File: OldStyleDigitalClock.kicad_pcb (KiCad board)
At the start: 2 copper layers, 155 x 85 mm, 89 parts, among them J1 USB_A_OUT, J2 USB_A_OUT, J3 USB_C_IN, SW1 Set minutes, SW2 Set hours, U1 CD4071BM, U10 CD4026BNSR, U11 NE555D, U12 CD4060BM, U13 CD4017BM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

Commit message: Reduced C13 value to avoid visible flickering
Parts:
- C13: value 0.047 uF -> 22 nF

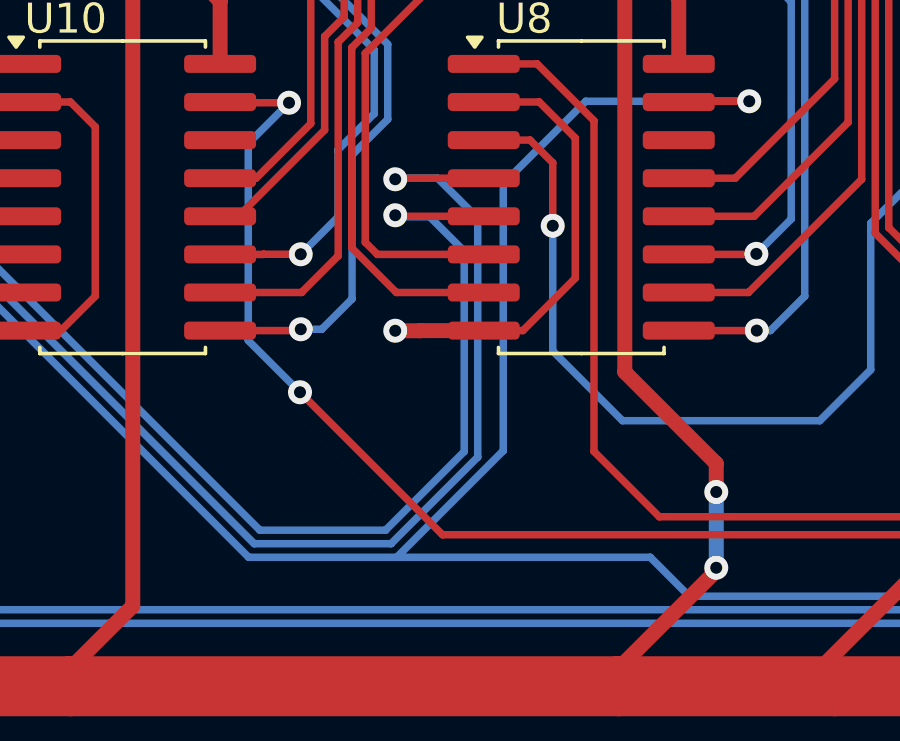
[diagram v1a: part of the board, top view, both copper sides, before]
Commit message: Added missing reset connection for low digit of the hours
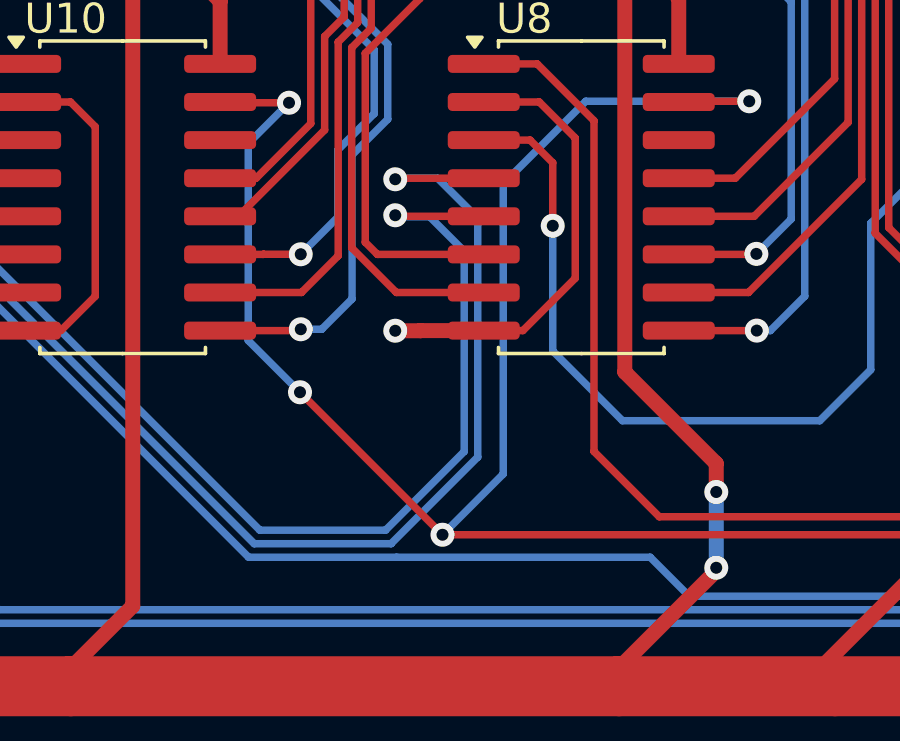
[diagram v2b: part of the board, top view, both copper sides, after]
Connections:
- U8 pad 15: MR -> Net-(U10-RESET)
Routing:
- net MR: track 192.2 -> 166.6 mm, vias 3 -> 2
- net Net-(U10-RESET): track 84.5 -> 108.7 mm, vias 2 -> 4

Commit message: Restored old Rs value of 300k
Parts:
- R_{S}1: value 200 kΩ -> 300 kΩ

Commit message: Reduced C13 to 4.7 nF to account for stray capacitance and avoid flickering
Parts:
- C13: value 22 nF -> 4.7 nF

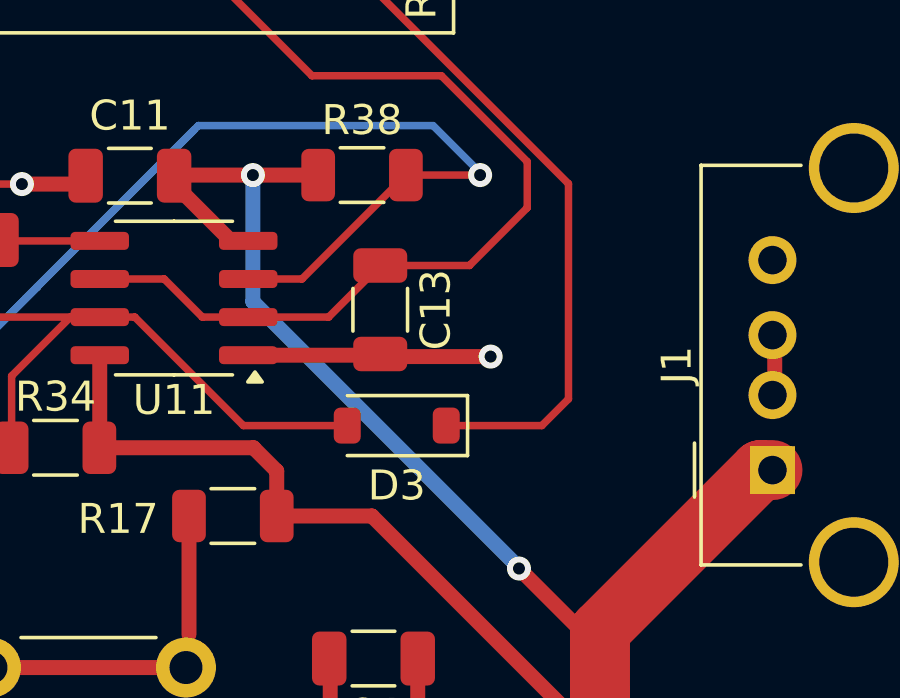
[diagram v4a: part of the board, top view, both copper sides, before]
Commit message: Minor PCB layout change to reduce traces stray capacitance
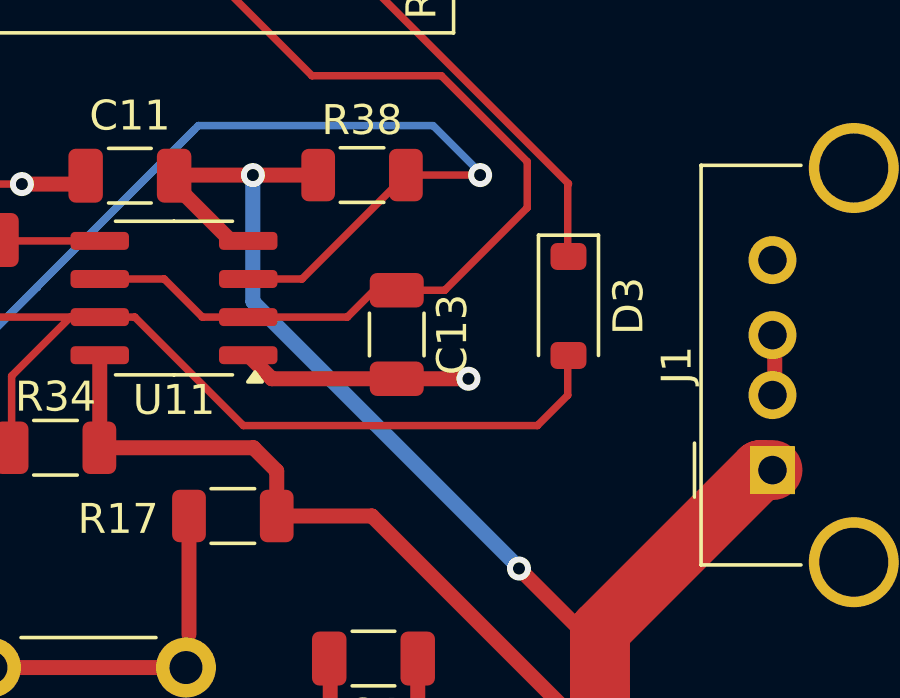
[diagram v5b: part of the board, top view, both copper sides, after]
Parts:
- moved D3 6.98 mm to (184.9, 70.5), turned to -90 degrees
- moved C13 0.99 mm to (179.2, 71.4)
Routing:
- net Net-(D3-K): track 26.7 -> 17.6 mm
- net Net-(D3-A): track 71.9 -> 81.0 mm

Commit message: Reduced C13 further while staying within the 555 limit of 100 kHz even when LDR may raise to several MΩ. This avoids flickering.
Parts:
- C13: value 4.7 nF -> 1 nF

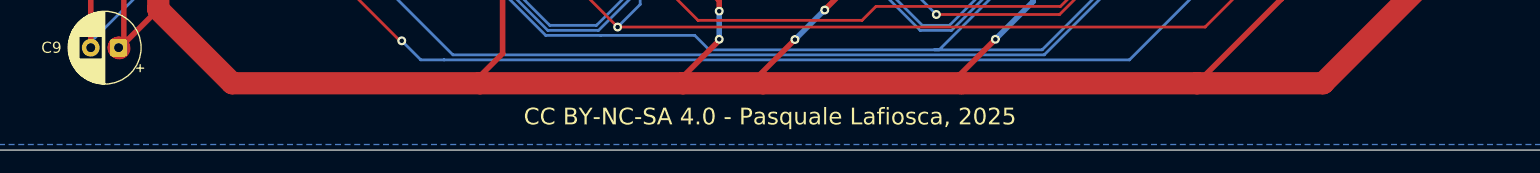
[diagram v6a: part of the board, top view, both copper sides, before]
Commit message: Added link in PCB description
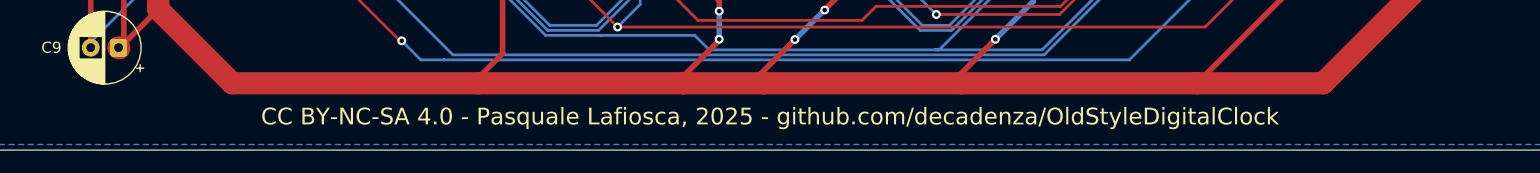
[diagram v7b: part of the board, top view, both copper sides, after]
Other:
- board text added: "CC BY-NC-SA 4.0 - Pasquale Lafiosca, 2025 - github.com/decadenza/OldStyleDigitalClock"
- board text removed: "CC BY-NC-SA 4.0 - Pasquale Lafiosca, 2025"
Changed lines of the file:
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@@
 		(layer "Edge.Cuts")
 	)
-	(gr_text "CC BY-NC-SA 4.0 - Pasquale Lafiosca, 2025"
+	(gr_text "CC BY-NC-SA 4.0 - Pasquale Lafiosca, 2025 - github.com/decadenza/OldStyleDigitalClock"
 		(at 127.5 132 0)
 		(layer "F.SilkS")
